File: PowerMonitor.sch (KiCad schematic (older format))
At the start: 2 parts

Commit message: schematic done
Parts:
- removed U?: ISO7331FC, Housings_SOIC:SOIC-16W_7.5x10.3mm_Pitch1.27mm, symbol ISO7331FC
- added C1, C2, C3, C4: 33nF 50V, Capacitors_SMD:C_0805, symbol C
- added C10, C11, C12, C13, C14, C5: 0.1uF 25V, Capacitors_SMD:C_0603, symbol C
- added C6, C9: 10uF 16V, Capacitors_SMD:C_1210, symbol C
- added C7, C8: 2.2uF 25V, Capacitors_SMD:C_0805, symbol C
- added D1, D3: 15V 1W, nightmechanic_pcb:DO-219AB, symbol D_Zener
- added D2, D4: 40V 1A, nightmechanic_pcb:DO-219AB, symbol D_Schottky
- added F1: Fuse, nightmechanic_pcb:Bel_MRT_Fuse, symbol Fuse
- added J1, J2, J3, J4, J5, J6, J7: Conn_01x01, Measurement_Points:Measurement_Point_Square-TH_Small, symbol Conn_01x01
- added J8: Conn_01x09, Pin_Headers:Pin_Header_Straight_1x09_Pitch2.54mm, symbol Conn_01x09
- added K1: T9AS5D12-5, nightmechanic_pcb:TE_T9AS_code1, symbol T9AS5D12-5
- added K2: KEMET_UA2_5NJ, nightmechanic_pcb:Kemet_UA2, symbol KEMET_UA2_5NJ
- added L1, L2, L3, L4: FB 300ohm, Capacitors_SMD:C_0805, symbol Ferrite_Bead
- added L5: 22uH, nightmechanic_pcb:Murata_8200, symbol L_Core_Iron
- added P1, P2, P3, P4: Keystone_4912, nightmechanic_pcb:Keystone_4912, symbol Keystone_4912
- added Q1, Q2, Q3: DMN3067LW, TO_SOT_Packages_SMD:SOT-23, symbol DMN3067LW
- added R1, R3, R4: 330k, Resistors_SMD:R_1206, symbol R
- added R10, R15, R16, R17, R18: 2.2k, Resistors_SMD:R_0603, symbol R
- added R11, R14: 4.7k, Resistors_SMD:R_0603, symbol R
- added R12: 0R, Resistors_SMD:R_0603, symbol R
- added R13: 10R, Resistors_SMD:R_0805, symbol R
- added R2, R7: 10k, Resistors_SMD:R_0603, symbol R
- added R5, R6, R8, R9: 1.5k, Resistors_SMD:R_0805, symbol R
- added RS1: OAR5R005, nightmechanic_pcb:TE_OAR5, symbol OAR5R005
- added RS2: OAR5R050, nightmechanic_pcb:TE_OAR5, symbol OAR5R050
- added RV1: Varistor, nightmechanic_pcb:Bourns_MOV_14D431K, symbol Varistor
- added U1: IRM-02-5S, nightmechanic_pcb:IRM-02-xS, symbol IRM-02-5S
- added U2: IRM-05-5, nightmechanic_pcb:IRM-05-x, symbol IRM-05-5
- added U4: LP5907MFX-3.3, TO_SOT_Packages_SMD:SOT-23-5, symbol LP5907MFX-3.3
- added U5: ISO7731FDBQ, nightmechanic_pcb:TI_DBQ0016A, symbol ISO7731FDBQ
- added U6: ISO1540D, nightmechanic_pcb:TI_ISO1540D8, symbol ISO1540D
- U3: renamed from U?; footprint Housings_DFN_QFN:QFN-28-1EP_5x5mm_Pitch0.5mm -> nightmechanic_pcb:QFN-28-1EP_5x5mm_Pitch0.5mm_mod
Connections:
- net MCP_EVENT: now reaches U3.1 (EVENT)
- net MCP_EVENT: now also J7.1 (Pin_1), Q3.1 (G), R7.1, U5.12 (INC)
- net at U3.10 (RESET\): now also R11.2
- net +3.3VA: now reaches U3.11 (AVDD)
- net +3.3VA: now also C5.1, C7.1, R11.1, R13.2
- net GNDD: now reaches U3.12 (A0)
- net GNDD: now also U3.15 (A1), U3.24 (DGND), U3.27 (DGND), U3.29 (PAD), C10.2, C11.2, C12.2, C6.2, C8.2, K1.3 (COM), L1.1, P2.1, Q1.2 (S), Q2.2 (S), Q3.2 (S), R12.1, R2.2, R7.2, RV1.2, U1.13 (-Vo), U1.24 (AC/N), U2.2 (AC/N), U4.2 (GND), U4.4 (NC), U5.15 (GND2), U5.9 (GND2), U6.5 (GND2)
- net at U3.13 (SCL): now also R15.2, U6.6 (SCL2)
- net at U3.14 (SDA): now also R16.2, U6.7 (SDA2)
- net at U3.16 (I1+): now also C3.1, R8.1
- net at U3.17 (I1-): now also C4.2, R9.1
- net at U3.18 (V1-): now also C1.1, R4.1, R5.1
- net at U3.19 (V1+): now also C2.2, R6.2
- net at U3.20 (AN_IN): now also J2.1 (Pin_1)
- net GNDA: now reaches U3.21 (AGND)
- net GNDA: now also C1.2, C2.1, C3.2, C4.1, C5.2, C7.2, L1.2, R12.2, R5.2, R6.1
- net at U3.22 (ZCD): now also J5.1 (Pin_1)
- net at U3.23 (REFIN/OUT+): now also J1.1 (Pin_1)
- net +3V3: now reaches U3.25 (DVDD)
- net +3V3: now also C10.1, C11.1, C12.1, C8.1, R13.1, R14.1, R15.1, R16.1, U4.5 (OUT), U5.10 (EN2), U5.16 (VCC2), U6.8 (VCC2)
- net MCP_MCLR: now reaches U3.26 (MCLR\)
- net MCP_MCLR: now also R14.2, U5.13 (OUTB)
- net at U3.4 (COMMON_B): now also U3.5 (COMMON_A), J6.1 (Pin_1)
- net at U3.6 (OSCI): now also J3.1 (Pin_1)
- net at U3.7 (OSCO): now also J4.1 (Pin_1)
- new net: F1.1, RV1.1, U1.1 (AC/L), U2.1 (AC/L)
- new net: C6.1, L5.2, U4.1 (IN), U4.3 (EN)
- new net: K2.7, P1.1, RS1.1
- new net: K2.5, P3.1, RS2.2
- new net: D2.2 (A), K1.1 (COIL1), Q1.3 (D)
- new net: K1.4 (NC), K2.2, RS1.2
- new net: K1.5 (NO), K2.4, RS2.1
- new net: D1.1 (K), D2.1 (K)
- new net: K2.3, L3.2
- new net: K2.6, L4.2
- new net: D4.2 (A), K2.8, Q2.3 (D)
- new net: D3.1 (K), D4.1 (K)
- new net: R1.1, R3.2
- new net: L2.1, R1.2
- new net: R3.1, R4.2
- new net: L3.1, R8.2
- new net: L4.1, R9.2
- new net +3.3V_ISO: C13.1, C14.1, J8.4 (Pin_4), R17.1, R18.1, U5.1 (VCC1), U5.7 (EN1), U6.1 (VCC1)
- new net +5V: D1.2 (A), D3.2 (A), K1.2 (COIL2), K2.1, L5.1, U1.12 (+Vo)
- new net +5V_ISO: C9.1, J8.1 (Pin_1), J8.2 (Pin_2), U2.3 (+Vo)
- new net EVENT_ISO: J8.9 (Pin_9), U5.5 (OUTC)
- new net GND: C13.2, C14.2, C9.2, J8.3 (Pin_3), U2.4 (-Vo), U5.2 (GND1), U5.8 (GND1), U6.4 (GND1)
- new net Line_In: F1.2, L2.2, P4.1
- new net MCLR_ISO: J8.8 (Pin_8), U5.4 (INB)
- new net SCL_ISO: J8.6 (Pin_6), R18.2, U6.3 (SCL1)
- new net SDA_ISO: J8.5 (Pin_5), R17.2, U6.2 (SDA1)
- new net SW_CRTL_RPI: R10.1, U5.14 (OUTA)
- new net SW_CTRL_ISO: J8.7 (Pin_7), U5.3 (INA)
- new net SW_CTRL_PROT: Q1.1 (G), Q2.1 (G), Q3.3 (D), R10.2, R2.1
- no-connect marks 0 -> 2
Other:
- moved on the sheet: U3

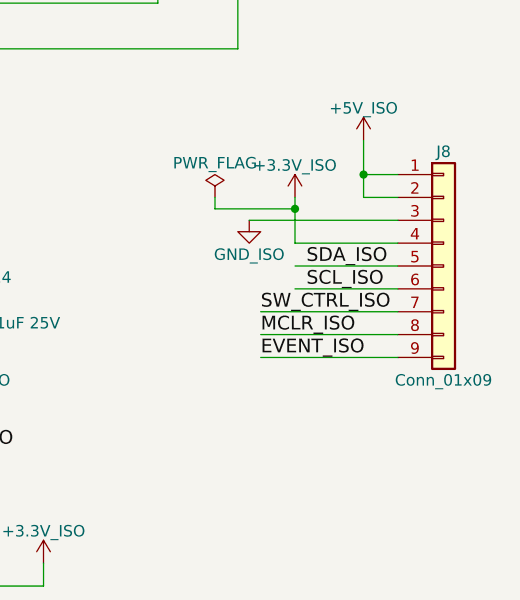
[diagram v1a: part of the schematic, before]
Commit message: another gnd_iso on connector
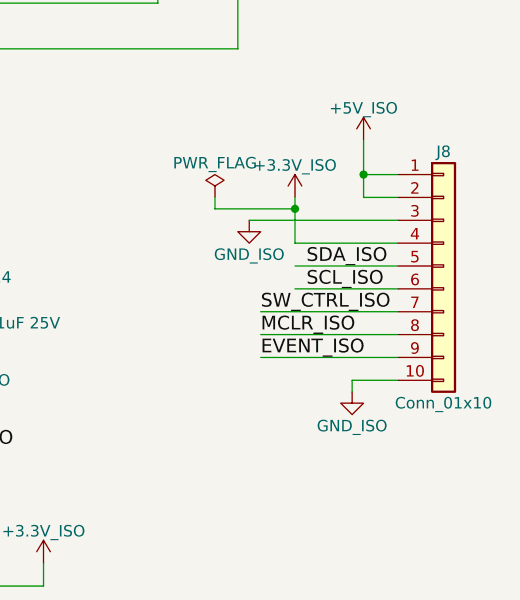
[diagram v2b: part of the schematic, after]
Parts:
- removed J8: Conn_01x09, Pin_Headers:Pin_Header_Straight_1x09_Pitch2.54mm, symbol Conn_01x09
- added J8: Conn_01x10, Pin_Headers:Pin_Header_Straight_1x10_Pitch2.54mm, symbol Conn_01x10
- Q1, Q2, Q3: footprint TO_SOT_Packages_SMD:SOT-23 -> TO_SOT_Packages_SMD:SOT-323_SC-70
- U4: footprint TO_SOT_Packages_SMD:SOT-23-5 -> nightmechanic_pcb:TI_DBV005
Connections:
- net +3.3V_ISO: now also J8.4 (Pin_4)
- net +5V_ISO: now also J8.1 (Pin_1), J8.2 (Pin_2)
- net EVENT_ISO: now also J8.9 (Pin_9)
- net GND: now also J8.10 (Pin_10), J8.3 (Pin_3)
- net MCLR_ISO: now also J8.8 (Pin_8)
- net SCL_ISO: now also J8.6 (Pin_6)
- net SDA_ISO: now also J8.5 (Pin_5)
- net SW_CTRL_ISO: now also J8.7 (Pin_7)
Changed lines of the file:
@@
 F 0 "U4" H 8950 3000 60  0000 C CNN
 F 1 "LP5907MFX-3.3" H 8950 2900 60  0000 C CNN
-F 2 "TO_SOT_Packages_SMD:SOT-23-5" H 8950 2650 60  0001 C CNN
+F 2 "nightmechanic_pcb:TI_DBV005" H 8950 2650 60  0001 C CNN
 F 3 "" H 8950 2650 60  0001 C CNN
 	1    8950 2650
@@
 F 0 "Q1" H 3800 4290 50  0000 R CNN
 F 1 "DMN3067LW" H 4280 4100 50  0000 R CNN
-F 2 "TO_SOT_Packages_SMD:SOT-23" H 3700 4300 50  0001 C CNN
+F 2 "TO_SOT_Packages_SMD:SOT-323_SC-70" H 3700 4300 50  0001 C CNN
 F 3 "" H 3500 4200 50  0000 C CNN
 	1    3500 4200
@@
 F 0 "Q3" H 5900 4590 50  0000 R CNN
 F 1 "DMN3067LW" H 6380 4400 50  0000 R CNN
-F 2 "TO_SOT_Packages_SMD:SOT-23" H 5800 4600 50  0001 C CNN
+F 2 "TO_SOT_Packages_SMD:SOT-323_SC-70" H 5800 4600 50  0001 C CNN
 F 3 "" H 5600 4500 50  0000 C CNN
 	1    5600 4500
@@
 F 0 "Q2" H 4100 8140 50  0000 R CNN
 F 1 "DMN3067LW" H 3750 7750 50  0000 R CNN
-F 2 "TO_SOT_Packages_SMD:SOT-23" H 4000 8150 50  0001 C CNN
+F 2 "TO_SOT_Packages_SMD:SOT-323_SC-70" H 4000 8150 50  0001 C CNN
 F 3 "" H 3800 8050 50  0000 C CNN
 	1    3800 8050
@@
 Wire Notes Line
 	12500 2150 12500 9400
-$Comp
-L Conn_01x09 J8
-U 1 1 5AEA6756
-P 15650 6700
-F 0 "J8" H 15650 7200 50  0000 C CNN
-F 1 "Conn_01x09" H 15650 6200 50  0000 C CNN
-F 2 "Pin_Headers:Pin_Header_Straight_1x09_Pitch2.54mm" H 15650 6700 50  0001 C CNN
-F 3 "" H 15650 6700 50  0001 C CNN
-	1    15650 6700
-	1    0    0    -1
-$EndComp
 $Comp
 L +5V_ISO #PWR034
@@
 $EndComp
 Connection ~ 1500 2350
+$Comp
+L Conn_01x10 J8
+U 1 1 5AE8F11D
+P 15650 6700
+F 0 "J8" H 15650 7200 50  0000 C CNN
+F 1 "Conn_01x10" H 15650 6100 50  0000 C CNN
+F 2 "Pin_Headers:Pin_Header_Straight_1x10_Pitch2.54mm" H 15650 6700 50  0001 C CNN
+F 3 "" H 15650 6700 50  0001 C CNN
+	1    15650 6700
+	1    0    0    -1
+$EndComp
+Wire Wire Line
+	15450 7200 15250 7200
+Wire Wire Line
+	15250 7200 15250 7250
+$Comp
+L GND_ISO #PWR050
+U 1 1 5AE8F345
+P 15250 7250
+F 0 "#PWR050" H 15250 7000 50  0001 C CNN
+F 1 "GND_ISO" H 15250 7100 50  0000 C CNN
+F 2 "" H 15250 7250 50  0001 C CNN
+F 3 "" H 15250 7250 50  0001 C CNN
+	1    15250 7250
+	1    0    0    -1
+$EndComp
 $EndSCHEMATC

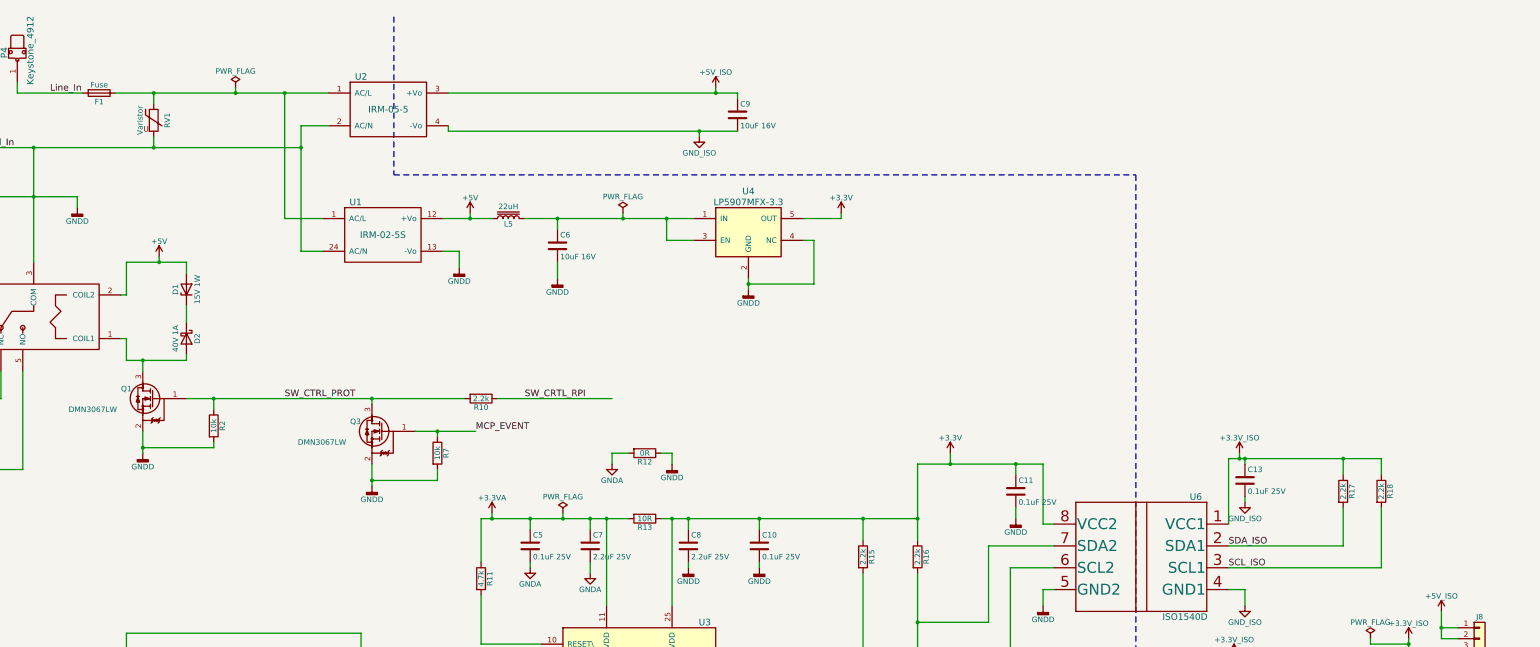
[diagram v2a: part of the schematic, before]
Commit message: added Live/isolated text
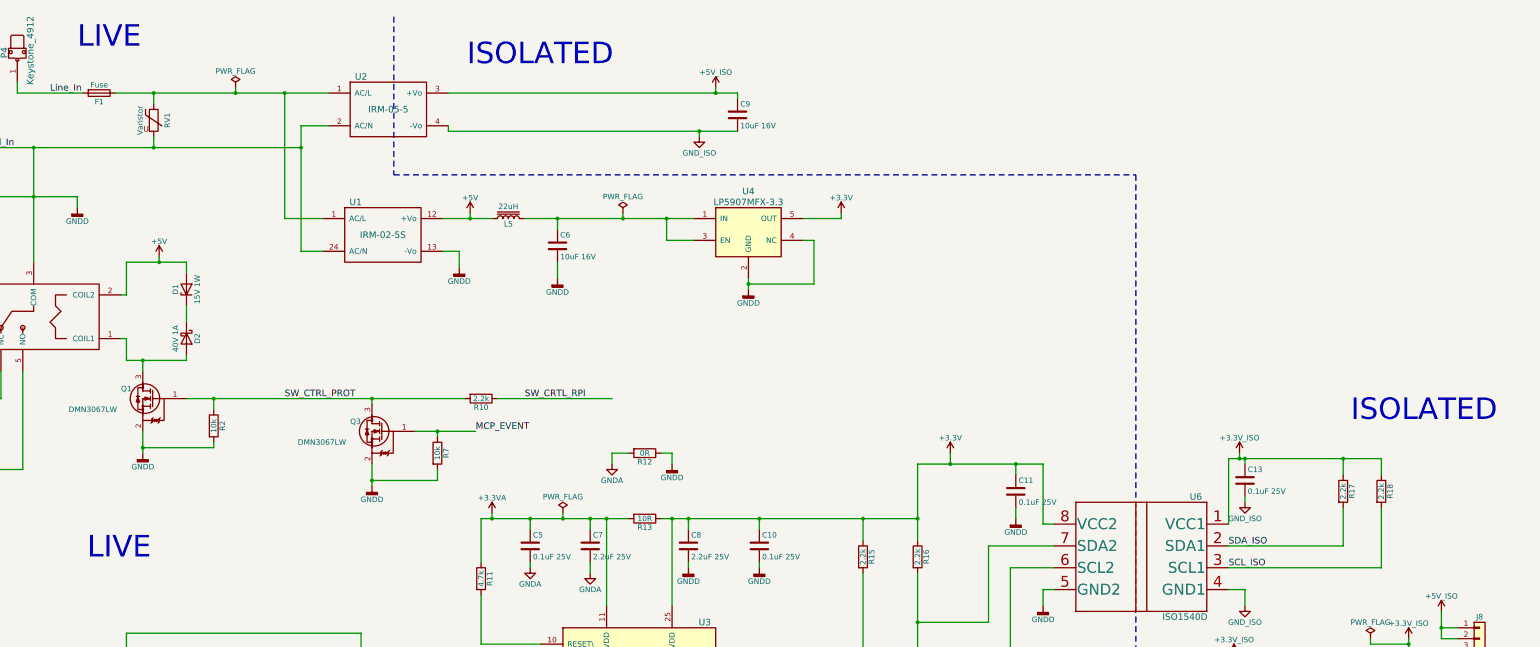
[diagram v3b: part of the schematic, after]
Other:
- note added: "ISOLATED\n"
- note added: "LIVE"
- note added: "LIVE\n"
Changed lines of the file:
@@
 	1    0    0    -1
 $EndComp
+Text Notes 6370 1160 0    197  ~ 0
+ISOLATED\n
+Text Notes 14470 4420 0    197  ~ 0
+ISOLATED\n
+Text Notes 2800 1000 0    197  ~ 0
+LIVE\n
+Text Notes 2890 5680 0    197  ~ 0
+LIVE
 $EndSCHEMATC

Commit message: initial placement
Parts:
- added D5, D6, D7, D8: LED, LEDs:LED_D3.0mm, symbol LED
- added J10, J11, J12, J13, J14, J15, J9: TEST_1P, nightmechanic_pcb:Keystone_50XX_TP, symbol TEST_1P
- added J16: Conn_01x03, Pin_Headers:Pin_Header_Straight_1x03_Pitch2.54mm, symbol Conn_01x03
- added R19, R21: 300R, Resistors_SMD:R_0805, symbol R
- added R20, R22: 120R, Resistors_SMD:R_0805, symbol R
- C10, C11, C12, C13, C14, C5: footprint Capacitors_SMD:C_0603 -> Capacitors_SMD:C_0805
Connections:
- net +3.3VA: now also J9.1
- net +3.3V_ISO: now also D8.2 (A), J15.1
- net +3V3: now also D6.2 (A), J14.1
- net +5V: now also D4.1 (K), D5.2 (A); no longer D3.2 (A)
- net +5V_ISO: now also D7.2 (A), J12.1
- net GND: now also J13.1, J16.3 (Pin_3), R21.1, R22.1
- net GNDA: now also J10.1
- net GNDD: now also J11.1, R19.1, R20.1
- net SCL_ISO: now also J16.2 (Pin_2)
- net SDA_ISO: now also J16.1 (Pin_1)
- net at P1.1, RS1.1: now also K2.2; no longer K2.7
- net at P3.1, RS2.2: now also K2.4; no longer K2.5
- net at K1.4 (NC), RS1.2: now also K2.7; no longer K2.2
- net at K1.5 (NO), RS2.1: now also K2.5; no longer K2.4
- net at K2.3: now also L4.2; no longer L3.2
- net at K2.6: now also L3.2; no longer L4.2
- net at K2.8, Q2.3 (D): now also D3.1 (K); no longer D4.2 (A)
- new net: D3.2 (A), D4.2 (A)
- new net: D7.1 (K), R21.2
- new net: D8.1 (K), R22.2
- new net: D5.1 (K), R19.2
- new net: D6.1 (K), R20.2
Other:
- moved on the sheet: Q2

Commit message: placwmwnt v0.2
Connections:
- net +5V: now also D2.1 (K); no longer D1.2 (A)
- net Line_In: no longer L2.2
- net Line_fused: now reaches F1.1, RV1.1, U1.1 (AC/L), U2.1 (AC/L)
- net Line_fused: now also L2.2
- net at K1.1 (COIL1), Q1.3 (D): now also D1.1 (K); no longer D2.2 (A)
- net at K2.3: now also L3.2; no longer L4.2
- net at K2.6: now also L4.2; no longer L3.2
- new net: D1.2 (A), D2.2 (A)
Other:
- moved on the sheet: D1, D2, D3, D4, Q2
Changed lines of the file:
@@
 L D_Schottky D2
 U 1 1 5AE26326
+P 3800 3200
+F 0 "D2" H 3800 3300 50  0000 C CNN
+F 1 "40V 1A" H 3800 3100 50  0000 C CNN
+F 2 "nightmechanic_pcb:DO-219AB" H 3800 3200 50  0001 C CNN
+F 3 "" H 3800 3200 50  0001 C CNN
+	1    3800 3200
+	0    1    1    0
+$EndComp
+$Comp
+L D_Zener D1
+U 1 1 5AE263AF
 P 3800 3650
-F 0 "D2" H 3800 3750 50  0000 C CNN
-F 1 "40V 1A" H 3800 3550 50  0000 C CNN
+F 0 "D1" H 3800 3750 50  0000 C CNN
+F 1 "15V 1W" H 3800 3550 50  0000 C CNN
 F 2 "nightmechanic_pcb:DO-219AB" H 3800 3650 50  0001 C CNN
 F 3 "" H 3800 3650 50  0001 C CNN
 	1    3800 3650
-	0    1    1    0
-$EndComp
-$Comp
-L D_Zener D1
-U 1 1 5AE263AF
-P 3800 3200
-F 0 "D1" H 3800 3300 50  0000 C CNN
-F 1 "15V 1W" H 3800 3100 50  0000 C CNN
-F 2 "nightmechanic_pcb:DO-219AB" H 3800 3200 50  0001 C CNN
-F 3 "" H 3800 3200 50  0001 C CNN
-	1    3800 3200
 	0    -1   -1   0
 $EndComp
@@
 L DMN3067LW Q2
 U 1 1 5AE26EEF
-P 4500 6750
-F 0 "Q2" H 4800 6840 50  0000 R CNN
-F 1 "DMN3067LW" H 4450 6450 50  0000 R CNN
-F 2 "TO_SOT_Packages_SMD:SOT-323_SC-70" H 4700 6850 50  0001 C CNN
-F 3 "" H 4500 6750 50  0000 C CNN
-	1    4500 6750
+P 3850 8100
+F 0 "Q2" H 4150 8190 50  0000 R CNN
+F 1 "DMN3067LW" H 3800 7800 50  0000 R CNN
+F 2 "TO_SOT_Packages_SMD:SOT-323_SC-70" H 4050 8200 50  0001 C CNN
+F 3 "" H 3850 8100 50  0000 C CNN
+	1    3850 8100
 	-1   0    0    -1
 $EndComp
@@
 L D_Schottky D4
 U 1 1 5AE26EF5
+P 4100 7100
+F 0 "D4" H 4100 7200 50  0000 C CNN
+F 1 "40V 1A" H 4100 7000 50  0000 C CNN
+F 2 "nightmechanic_pcb:DO-219AB" H 4100 7100 50  0001 C CNN
+F 3 "" H 4100 7100 50  0001 C CNN
+	1    4100 7100
+	0    1    1    0
+$EndComp
+$Comp
+L D_Zener D3
+U 1 1 5AE26EFB
 P 4100 7550
-F 0 "D4" H 4100 7650 50  0000 C CNN
-F 1 "40V 1A" H 4100 7450 50  0000 C CNN
+F 0 "D3" H 4100 7650 50  0000 C CNN
+F 1 "15V 1W" H 4100 7450 50  0000 C CNN
 F 2 "nightmechanic_pcb:DO-219AB" H 4100 7550 50  0001 C CNN
 F 3 "" H 4100 7550 50  0001 C CNN
 	1    4100 7550
-	0    1    -1   0
-$EndComp
-$Comp
-L D_Zener D3
-U 1 1 5AE26EFB
-P 4100 7100
-F 0 "D3" H 4100 7200 50  0000 C CNN
-F 1 "15V 1W" H 4100 7000 50  0000 C CNN
-F 2 "nightmechanic_pcb:DO-219AB" H 4100 7100 50  0001 C CNN
-F 3 "" H 4100 7100 50  0001 C CNN
-	1    4100 7100
-	0    -1   1    0
+	0    -1   -1   0
 $EndComp
 $Comp
@@
 L +5V #PWR013
 U 1 1 5AE93E30
-P 3750 7650
-F 0 "#PWR013" H 3750 7500 50  0001 C CNN
-F 1 "+5V" H 3750 7790 50  0000 C CNN
-F 2 "" H 3750 7650 50  0001 C CNN
-F 3 "" H 3750 7650 50  0001 C CNN
-	1    3750 7650
+P 3850 6700
+F 0 "#PWR013" H 3850 6550 50  0001 C CNN
+F 1 "+5V" H 3850 6840 50  0000 C CNN
+F 2 "" H 3850 6700 50  0001 C CNN
+F 3 "" H 3850 6700 50  0001 C CNN
+	1    3850 6700
 	1    0    0    -1
 $EndComp
@@
 L GNDD #PWR014
 U 1 1 5AE94194
-P 4400 7150
-F 0 "#PWR014" H 4400 6900 50  0001 C CNN
-F 1 "GNDD" H 4400 7025 50  0000 C CNN
-F 2 "" H 4400 7150 50  0001 C CNN
-F 3 "" H 4400 7150 50  0001 C CNN
-	1    4400 7150
+P 3750 8500
+F 0 "#PWR014" H 3750 8250 50  0001 C CNN
+F 1 "GNDD" H 3750 8375 50  0000 C CNN
+F 2 "" H 3750 8500 50  0001 C CNN
+F 3 "" H 3750 8500 50  0001 C CNN
+	1    3750 8500
 	1    0    0    -1
 $EndComp
@@
 Text Label 4700 4200 0    60   ~ 0
 SW_CTRL_PROT
-Text Label 4800 6750 0    60   ~ 0
+Text Label 4150 8100 0    60   ~ 0
 SW_CTRL_PROT
 $Comp
@@
 $EndComp
 Text Label 2000 9600 0    60   ~ 0
-Line_In
+Line_fused
 $Comp
 L GNDA #PWR018
@@
 Connection ~ 5500 4950
 Wire Wire Line
-	3500 6900 3500 6800
-Wire Wire Line
-	3500 6800 4100 6800
-Wire Wire Line
 	4100 6800 4100 6950
 Wire Wire Line
@@
 	4100 7750 4100 7700
 Wire Wire Line
-	3500 7750 4100 7750
-Wire Wire Line
-	3500 7750 3500 7600
-Wire Wire Line
-	4400 7050 4400 7150
+	3750 8400 3750 8500
 Wire Wire Line
 	2050 2350 2800 2350
@@
 Wire Wire Line
 	3250 6900 3250 6350
-Wire Wire Line
-	3250 6350 5400 6350
-Wire Wire Line
-	5400 6350 5400 7050
-Wire Wire Line
-	5400 8700 5400 7450
-Wire Wire Line
-	3250 8700 5400 8700
 Wire Wire Line
 	3250 8700 3250 7600
@@
 	14650 6900 14650 7000
 Wire Wire Line
-	3750 7650 3750 7750
-Connection ~ 3750 7750
-Wire Wire Line
-	4400 6500 4400 6450
-Wire Wire Line
-	4400 6450 3800 6450
-Wire Wire Line
-	3800 6450 3800 6800
-Connection ~ 3800 6800
-Wire Wire Line
 	3150 7900 1900 7900
 Wire Wire Line
@@
 Wire Wire Line
 	1250 6500 3350 6500
+Wire Wire Line
+	3850 6700 3850 7600
+Wire Wire Line
+	3850 6800 4100 6800
+Wire Wire Line
+	3750 7750 4100 7750
+Wire Wire Line
+	3500 6900 3500 6850
+Wire Wire Line
+	3500 6850 3750 6850
+Wire Wire Line
+	3750 6850 3750 7850
+Connection ~ 3750 7750
+Wire Wire Line
+	3850 7600 3500 7600
+Connection ~ 3850 6800
+Wire Wire Line
+	5400 7050 5150 7050
+Wire Wire Line
+	5150 7050 5150 8700
+Wire Wire Line
+	5150 8700 3250 8700
+Wire Wire Line
+	3250 6350 5000 6350
+Wire Wire Line
+	5000 6350 5000 7450
+Wire Wire Line
+	5000 7450 5400 7450
+Text Label 3950 1400 0    60   ~ 0
+Line_fused
 $EndSCHEMATC
